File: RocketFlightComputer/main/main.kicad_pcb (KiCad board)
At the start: 4 copper layers, 53.7 x 53.7 mm, 148 parts, among them J1 BATT, Q2 SI2302, Q3 SI2302, Q4 SI2302, Y1 32.768kHz, Y2 24MHz, Y3 32.768kHz, Y4 32.768kHz

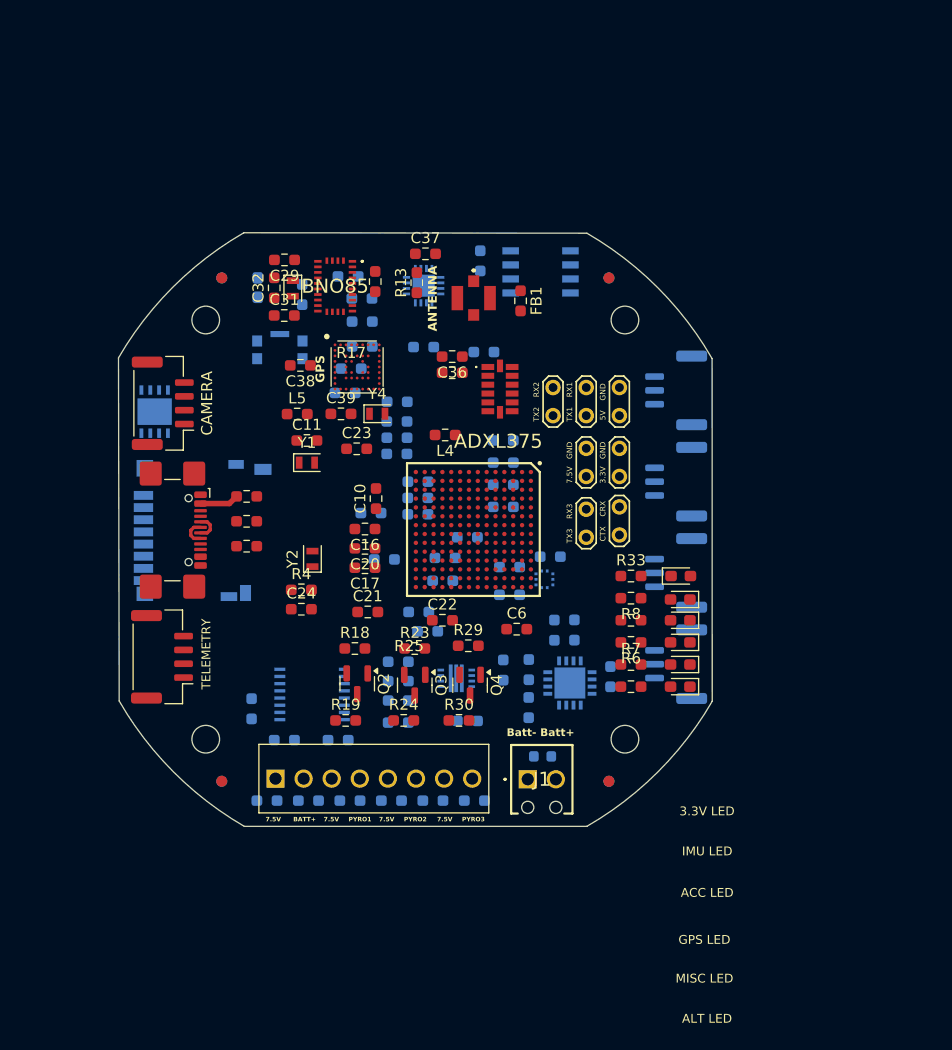
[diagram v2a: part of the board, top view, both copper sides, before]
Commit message: Preliminary layout done but need to rearrange sd card and such to have the best routing
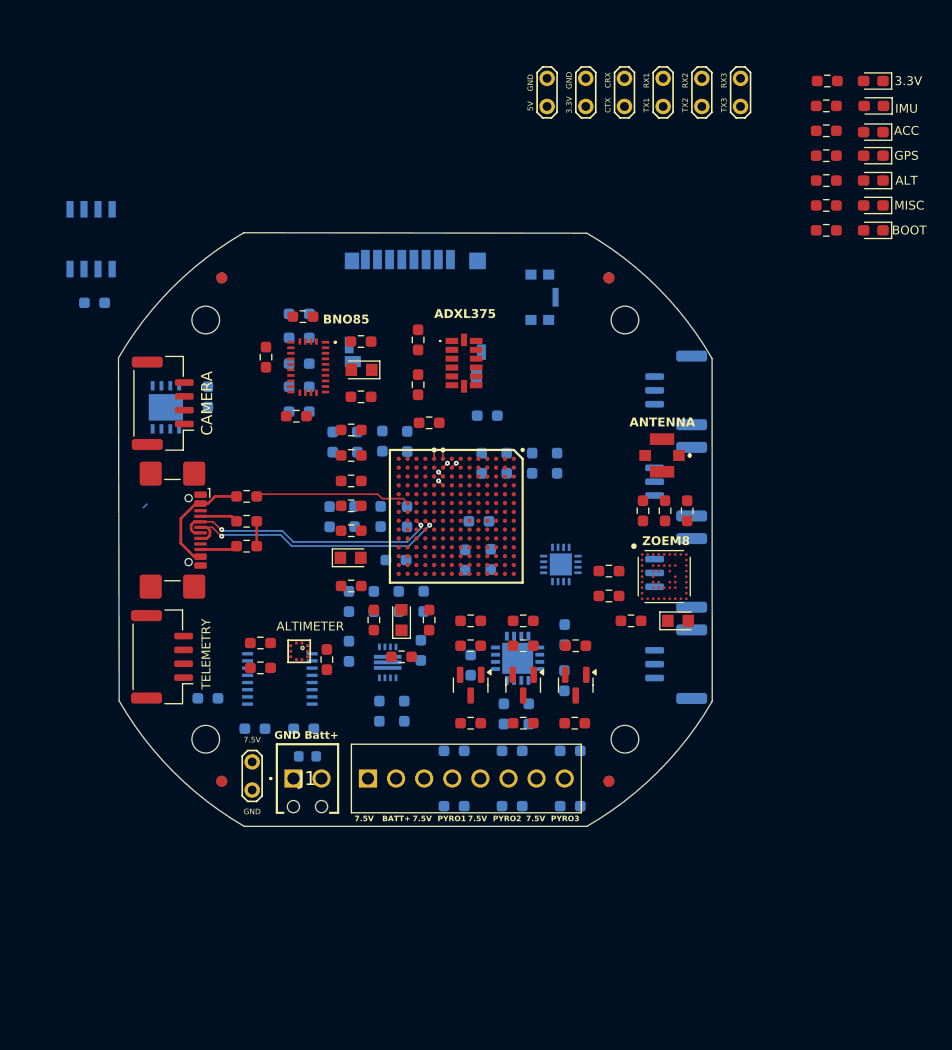
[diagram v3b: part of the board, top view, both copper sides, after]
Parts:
- BMP390, C33, C34, D1, R11, R2, R35: moved to F.Cu
- U-BLOX_ZOE_M8Q-0-10: value GPS -> ZOEM8
- Y1, Y2, Y3, Y4: footprint Crystal:Crystal_SMD_2012-2Pin_2.0x1.2mm -> footprint:830050789
- moved D1 58.7 mm to (151.3, 18.0), turned to 180 degrees
- moved R2 51.2 mm to (147.1, 18.0), turned to 0 degrees
- moved R5 46.9 mm to (147.0, 29.2)
- moved D4 46.9 mm to (151.3, 29.2)
- moved R33 46.0 mm to (147.0, 20.2)
- moved D8 45.9 mm to (151.3, 20.2), turned to 180 degrees
- moved R8 45.8 mm to (147.0, 22.5)
- moved D2 45.7 mm to (151.3, 22.6)
- moved R3 45.6 mm to (147.0, 24.7)
- moved D3 45.5 mm to (151.3, 24.7)
- moved R6 45.3 mm to (147.0, 27.0)
- moved D5 45.2 mm to (151.3, 27.0)
- moved R7 43.0 mm to (147.0, 31.5)
- moved D6 43.0 mm to (151.3, 31.5)
- moved TP6 41.4 mm to (139.3, 20.3)
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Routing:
- net /D+: track 2.44 -> 25.2 mm, vias 0 -> 2
- net /D-: track 2.44 -> 24.4 mm, vias 0 -> 2
- net Net-(MIMXRT1062DVL6B1-USB_OTG1_VBUS): track 0.00 -> 14.1 mm
- net Net-(L1-Pad1): track 3.52 -> 10.4 mm
- net Net-(USB_C_Receptacle_USB2.0_14P1-CC1): track 0.00 -> 3.44 mm
- net Net-(USB_C_Receptacle_USB2.0_14P1-CC2): track 0.00 -> 3.38 mm
- net GNDREF: track 0.00 -> 2.25 mm
- net /SD_B0_05: track 0.00 -> 1.00 mm, vias 0 -> 1
- net /SD_B0_03: track 0.00 -> 0.80 mm, vias 0 -> 1
- net /SD_B0_02: track 0.00 -> 0.80 mm, vias 0 -> 1
- net /SD_B0_04: track 0.00 -> 0.57 mm, vias 0 -> 1
- net /SD_B0_01: track 0.00 -> 0.57 mm, vias 0 -> 1
- net /SD_B0_00: track 0.00 -> 0.57 mm, vias 0 -> 1
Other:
- board text added: "3.3V"
- board text added: "ACC"
- board text added: "ALT"
- board text added: "BOOT"
- board text added: "GND"
- board text added: "GND Batt+"
- board text added: "GPS"
- board text added: "IMU"
- board text added: "MISC"
- board text removed: "3.3V LED"
- board text removed: "7.5V GND"
- board text removed: "ACC LED"
- board text removed: "ALT LED"
- board text removed: "Batt- Batt+"
- board text removed: "GPS LED"
- board text removed: "IMU LED"
- board text removed: "LED"
- board text removed: "MISC LED"

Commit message: Routing pcb
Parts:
- BMP390, C33, C34, R11: moved to B.Cu
- moved D8 75.9 mm to (97.3, 73.5)
- moved D2 72.7 mm to (97.3, 71.2), turned to 0 degrees
- moved R33 70.0 mm to (101.6, 73.5), turned to 180 degrees
- moved D3 69.8 mm to (97.3, 69.0), turned to 0 degrees
- moved D5 67.0 mm to (97.3, 66.7), turned to 0 degrees
- moved R8 66.7 mm to (101.6, 71.2), turned to 0 degrees
- moved R3 63.4 mm to (101.6, 69.0), turned to 0 degrees
- moved R6 60.4 mm to (101.6, 66.7), turned to 0 degrees
- moved C4 47.3 mm to (126.1, 51.8)
- moved 878-APS6404L-3SQR-SN1 46.9 mm to (125.1, 46.8)
- moved KMR241GLFS1 45.8 mm to (86.9, 68.0)
- moved D1 34.9 mm to (127.4, 43.4), turned to 0 degrees
- moved R2 34.9 mm to (123.2, 43.4)
- moved TP7 34.4 mm to (98.6, 36.8)
- moved TP3 31.1 mm to (95.4, 36.8)
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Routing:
- net /SD_B0_00: track 0.57 -> 21.4 mm
- net /SD_B0_01: track 0.57 -> 21.2 mm
- net /SD_B0_03: track 0.80 -> 20.6 mm
- net /SD_B0_02: track 0.80 -> 20.5 mm
- net /SD_B0_04: track 0.57 -> 19.2 mm
- net /SD_B0_05: track 1.00 -> 19.3 mm
- net GNDREF: track 2.25 -> 15.7 mm, vias 0 -> 2
- net Net-(MIMXRT1062DVL6B1-RTC_XTALI): track 0.00 -> 7.85 mm
- net Net-(U-BLOX_ZOE_M8Q-0-10-V_CORE): track 0.00 -> 6.49 mm
- net Net-(C10-Pad2): track 0.00 -> 6.23 mm
- net +3.3V: track 0.00 -> 6.13 mm, vias 0 -> 2
- net Net-(D3-A): track 0.00 -> 2.53 mm
- net /3.3v_led: track 0.00 -> 2.51 mm
- net Net-(D2-A): track 0.00 -> 2.47 mm
- net Net-(D5-A): track 0.00 -> 2.46 mm
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
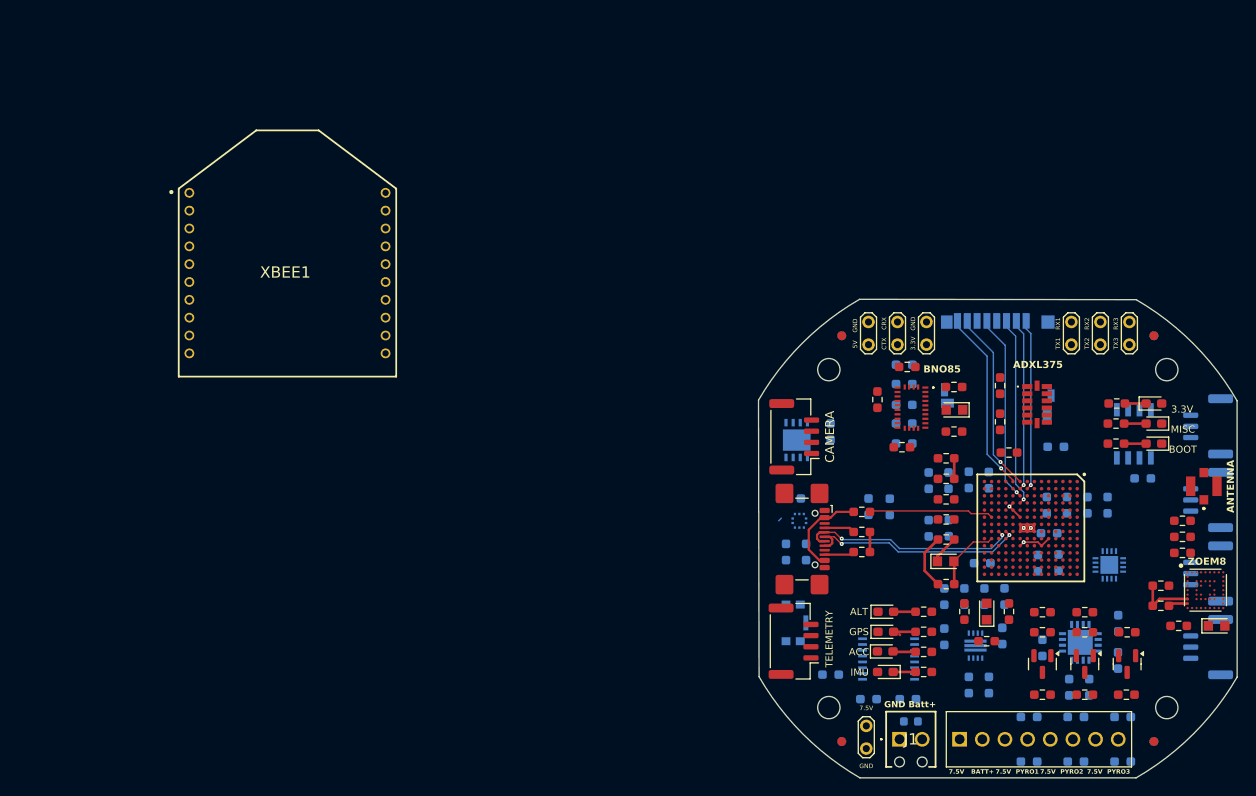
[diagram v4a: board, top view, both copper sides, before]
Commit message: Addition of teensy example and milestone on routing completed, missing a few components to connect
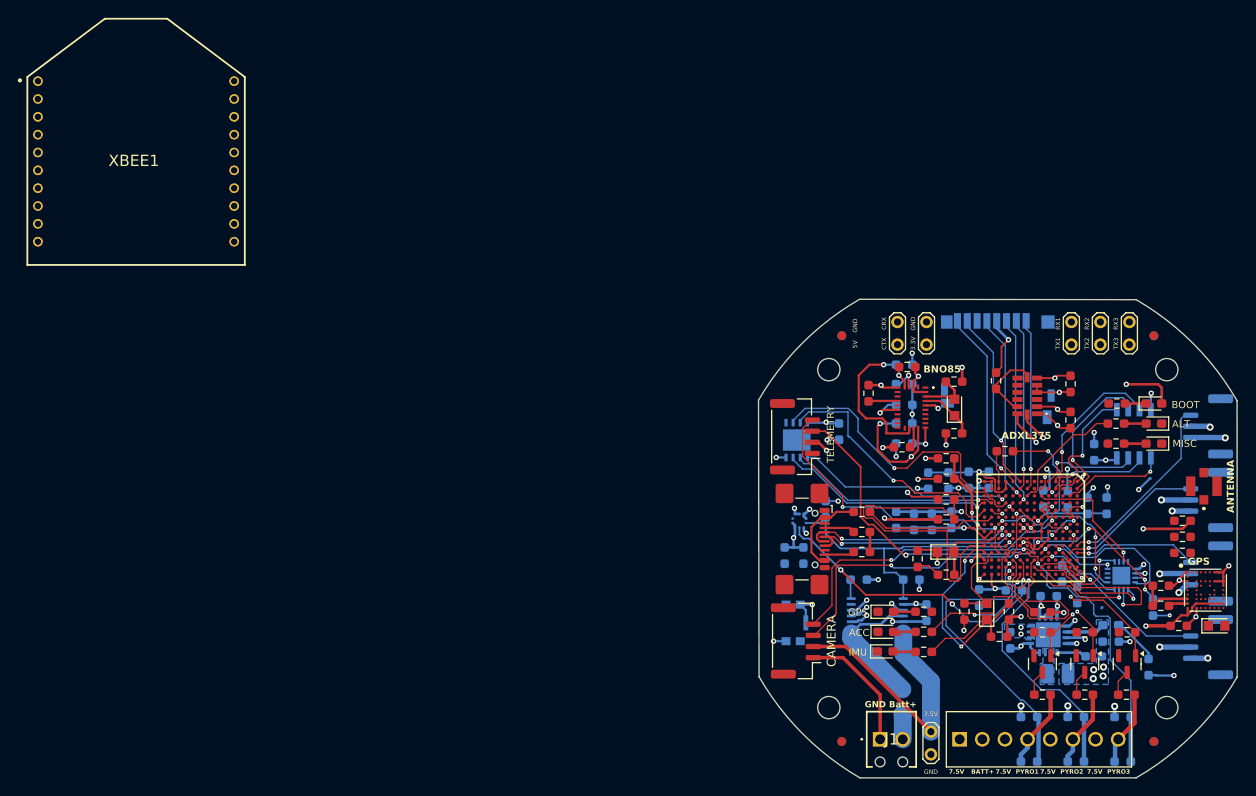
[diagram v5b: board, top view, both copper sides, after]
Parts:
- removed C41: 10uF, Resistor_SMD:R_0603_1608Metric_Pad0.98x0.95mm_HandSolder
- removed C42, C43: 22uF, Resistor_SMD:R_0603_1608Metric_Pad0.98x0.95mm_HandSolder
- removed C44: 3.3nF, Resistor_SMD:R_0603_1608Metric_Pad0.98x0.95mm_HandSolder
- removed L6: 1.5uH, Resistor_SMD:R_0603_1608Metric_Pad0.98x0.95mm_HandSolder
- removed R22: 470k, Resistor_SMD:R_0603_1608Metric_Pad0.98x0.95mm_HandSolder
- removed R25: 510k, Resistor_SMD:R_0603_1608Metric_Pad0.98x0.95mm_HandSolder
- removed R26: 82k, Resistor_SMD:R_0603_1608Metric_Pad0.98x0.95mm_HandSolder
- removed TP3: TestPoint_2Pole, TestPoint:TestPoint_2Pads_Pitch2.54mm_Drill0.8mm
- removed TPS621361RGXT1: 5Vreg, footprint:TPS621361RGXT
- C6, D8, R33: moved to B.Cu
- F2: value 5A -> 6A; footprint Fuse:Fuse_0603_1608Metric -> Fuse:Fuse_1206_3216Metric
- L2: footprint Resistor_SMD:R_0603_1608Metric_Pad0.98x0.95mm_HandSolder -> Inductor_SMD:L_1008_2520Metric_Pad1.43x2.20mm_HandSolder
- R14: moved to F.Cu
- R19, R24, R30: value 4 -> 7
- U-BLOX_ZOE_M8Q-0-10: value ZOEM8 -> GPS
- Y1, Y3: footprint footprint:830050789 -> Crystal:Crystal_SMD_2012-2Pin_2.0x1.2mm_HandSoldering
- moved D8 25.8 mm to (122.5, 68.2)
- moved R33 25.2 mm to (126.8, 72.9), turned to 90 degrees
- moved S4B-PH-K-S_LF__SN_1 22.9 mm to (87.1, 47.1)
- moved S4B-PH-K-S_LF__SN_2 22.9 mm to (87.2, 70.0)
- moved XBEE1 21.1 mm to (13.3, 0.25)
- moved R9 19.8 mm to (127.3, 66.3), turned to 90 degrees
- moved R166 14.5 mm to (94.3, 63.1), turned to 180 degrees
- moved R177 14.2 mm to (100.2, 63.1)
- moved C40 12.8 mm to (101.9, 66.8), turned to -90 degrees
- moved C6 12.0 mm to (107.8, 65.2), turned to -90 degrees
- moved R14 9.98 mm to (109.7, 40.8), turned to -90 degrees
- moved C35 8.97 mm to (118.0, 41.2), turned to -90 degrees
- moved C36 8.79 mm to (118.0, 45.2), turned to 90 degrees
- moved C3 8.38 mm to (115.6, 65.0), turned to 0 degrees
- moved R34 7.51 mm to (111.7, 64.3)
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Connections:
- C11 pad 1: GNDREF -> Net-(C10-Pad2)
- C11 pad 2: Net-(C10-Pad2) -> GNDREF
- C22 pad 1: Net-(MIMXRT1062DVL6B1-VDD_SNVS_CAP) -> GNDREF
- C22 pad 2: GNDREF -> Net-(MIMXRT1062DVL6B1-VDD_SNVS_CAP)
- C40 pad 1: +5V -> +3.3V
- INA260 pad 10: +5V -> +3.3V
- INA260 pad 7: /CURRENT VOLTAGE SENSOR/ALERT -> unconnected-(INA260-ALERT-Pad7)
- L4 pad 1: /M1M2 -> Net-(MIMXRT1062DVL6B1-DCDC_LP_1)
- L4 pad 2: Net-(MIMXRT1062DVL6B1-DCDC_LP_1) -> /M1M2
- MIMXRT1062DVL6B1 pad A10: unconnected-(MIMXRT1062DVL6B1-GPIO_B0_11-PadA10) -> /Servo4_PWM
- MIMXRT1062DVL6B1 pad A11: /Servo4_PWM -> /Servo2_PWM
- MIMXRT1062DVL6B1 pad C11: unconnected-(MIMXRT1062DVL6B1-GPIO_B1_02-PadC11) -> /Servo1_PWM
- MIMXRT1062DVL6B1 pad D9: /Servo2_PWM -> unconnected-(MIMXRT1062DVL6B1-GPIO_B0_10-PadD9)
- MIMXRT1062DVL6B1 pad E7: unconnected-(MIMXRT1062DVL6B1-GPIO_B0_01-PadE7) -> /PyroCH3_4
- MIMXRT1062DVL6B1 pad E8: unconnected-(MIMXRT1062DVL6B1-GPIO_B0_02-PadE8) -> /PyroCH2_3
- MIMXRT1062DVL6B1 pad G5: /PyroCH2_3 -> unconnected-(MIMXRT1062DVL6B1-GPIO_EMC_05-PadG5)
- MIMXRT1062DVL6B1 pad H3: /Servo1_PWM -> Net-(MIMXRT1062DVL6B1-GPIO_EMC_08)
- MIMXRT1062DVL6B1 pad H4: Net-(MIMXRT1062DVL6B1-GPIO_EMC_07) -> unconnected-(MIMXRT1062DVL6B1-GPIO_EMC_07-PadH4)
- MIMXRT1062DVL6B1 pad H5: /PyroCH3_4 -> unconnected-(MIMXRT1062DVL6B1-GPIO_EMC_06-PadH5)
- R10 pad 1: Net-(BNO85-BOOTN) -> +3.3V
- R10 pad 2: +3.3V -> Net-(BNO85-BOOTN)
- R12 pad 1: +3.3V -> Net-(BNO85-NRST)
- R12 pad 2: Net-(BNO85-NRST) -> +3.3V
- R3 pad 2: Net-(MIMXRT1062DVL6B1-GPIO_EMC_07) -> Net-(MIMXRT1062DVL6B1-GPIO_AD_B1_15)
- R5 pad 2: Net-(MIMXRT1062DVL6B1-GPIO_AD_B1_15) -> Net-(MIMXRT1062DVL6B1-GPIO_EMC_08)
- R8 pad 1: Net-(D2-A) -> Net-(MIMXRT1062DVL6B1-GPIO_AD_B1_14)
- R8 pad 2: Net-(MIMXRT1062DVL6B1-GPIO_AD_B1_14) -> Net-(D2-A)
- ScrewTerminal1 pad 1: /HighCurrentComponents/7.5V_AftSwitch -> +7.5V
- ScrewTerminal1 pad 2: +7.5V -> /HighCurrentComponents/7.5V_AftSwitch
- TPS62111RSAR1 pad 17: unconnected-(TPS62111RSAR1-EP-Pad17) -> GNDREF
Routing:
- net GNDREF: track 15.7 -> 175.0 mm, vias 2 -> 65
- net +7.5V: track 0.00 -> 134.6 mm, vias 0 -> 7
- net +3.3V: track 6.13 -> 101.2 mm, vias 2 -> 33
- net /Cam_TX: track 0.00 -> 40.8 mm, vias 0 -> 2
- net /BMP390_SDA1: track 0.00 -> 38.7 mm, vias 0 -> 3
- net Net-(MIMXRT1062DVL6B1-NVCC_PLL): track 0.00 -> 36.9 mm
- net /Cam_RX: track 0.00 -> 35.5 mm, vias 0 -> 2
- net /Pyro1_Test_40: track 0.00 -> 34.9 mm, vias 0 -> 1
- net /Xbee_RX: track 0.00 -> 34.4 mm, vias 0 -> 2
- net /BMO085_SCL: track 0.00 -> 33.8 mm, vias 0 -> 3
- net /BMP390_SCL1: track 0.00 -> 33.8 mm, vias 0 -> 1
- net /CLK: track 0.00 -> 33.6 mm, vias 0 -> 1
- net /Xbee_TX: track 0.00 -> 33.3 mm, vias 0 -> 2
- net Net-(MIMXRT1062DVL6B1-GPIO_AD_B1_14): track 0.00 -> 32.0 mm
- net /Pyro2_Test_41: track 0.00 -> 31.9 mm, vias 0 -> 1
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- added copper zone on B.Cu, net +3.3V
- added copper zone on In2.Cu, net +3.3V
- added copper zone on B.Cu, net +7.5V
- added copper zone on B.Cu, net Net-(TPS62111RSAR1-SW_1)

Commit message: First iteration of layout finished, we could call this v0, congratulations! Need an expert to state if layer 4 and layer 3 interations are ok (pwm/ psram/i2c/uart vs power plane 7.5v and 3.3v )
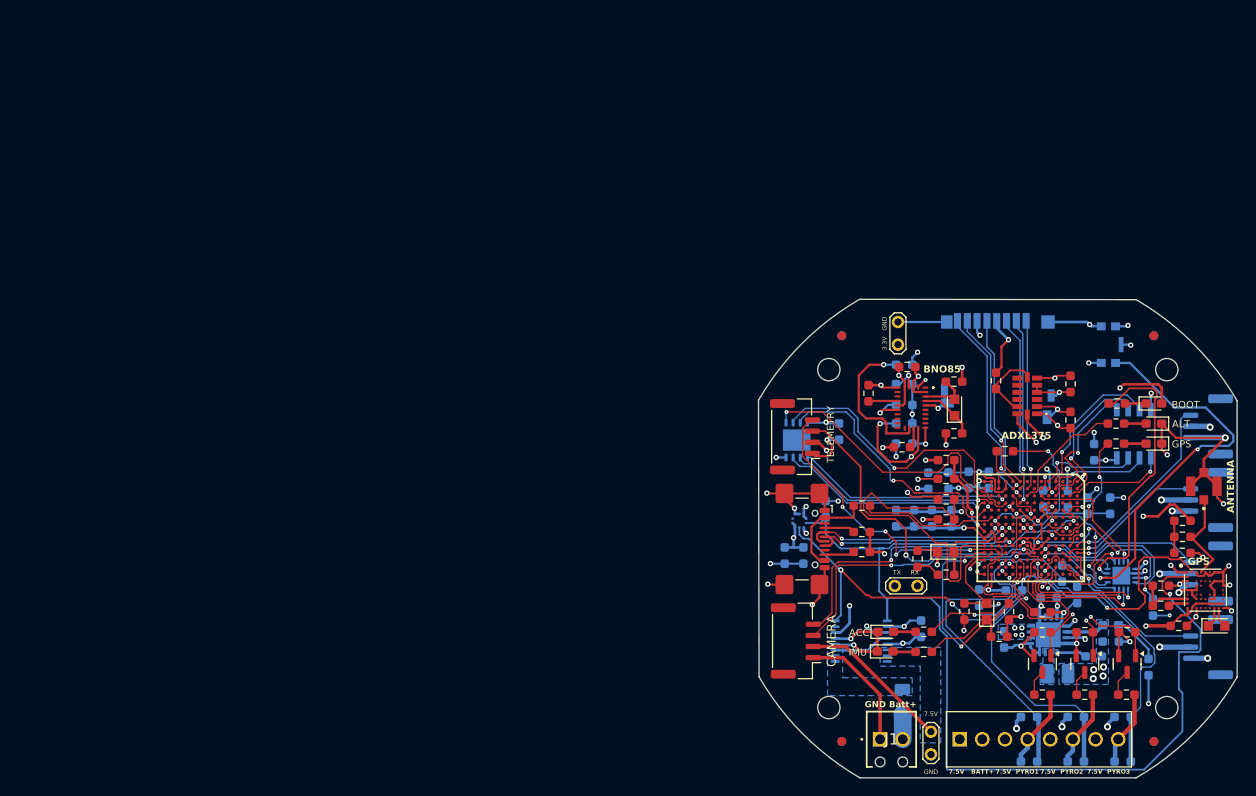
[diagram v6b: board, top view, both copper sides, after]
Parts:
- removed D5: GPS LED, LED_SMD:LED_0603_1608Metric_Pad1.05x0.95mm_HandSolder
- removed R166, R177: 10K, Resistor_SMD:R_0603_1608Metric_Pad0.98x0.95mm_HandSolder
- removed R6: 470, Resistor_SMD:R_0603_1608Metric_Pad0.98x0.95mm_HandSolder
- removed TP4, TP6, TP7: TestPoint_2Pole, TestPoint:TestPoint_2Pads_Pitch2.54mm_Drill0.8mm
- removed XBEE1: XB24CAPIT-001, footprint:XB24CAPIT-001
- D3: value 200G ACC LED -> GPS
- D6: value Misc LED -> 200G ACC LED
- moved KMR241GLFS1 47.2 mm to (122.3, 36.8)
- moved TP5 35.5 mm to (98.3, 63.8), turned to 0 degrees
- moved TP1 3.20 mm to (98.7, 36.8)
- moved INA260 3.08 mm to (94.6, 70.0)
- moved C40 1.90 mm to (101.3, 68.6)
- moved C1 0.71 mm to (110.6, 69.8)
- moved L1 0.70 mm to (94.6, 54.8)
- moved C14 0.40 mm to (102.5, 56.3)
- moved C28 0.40 mm to (122.5, 54.9)
- moved C9 0.40 mm to (100.5, 56.3)
- moved C16 0.21 mm to (104.1, 49.7)
- moved C7 0.18 mm to (98.5, 56.3)
- moved C18 0.17 mm to (104.7, 56.3)
- moved C3 0.15 mm to (115.6, 65.1)
- turned C13 to -90 degrees
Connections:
- net /Reserve_RX2 renamed /Reserve_RX
- net /Reserve_TX2 renamed /Reserve_TX
- MIMXRT1062DVL6B1 pad C10: Net-(MIMXRT1062DVL6B1-GPIO_B0_12) -> unconnected-(MIMXRT1062DVL6B1-GPIO_B0_12-PadC10)
- MIMXRT1062DVL6B1 pad H13: /Reserve_CTX -> unconnected-(MIMXRT1062DVL6B1-GPIO_AD_B1_08-PadH13)
- MIMXRT1062DVL6B1 pad J13: /Reserve_RX1 -> unconnected-(MIMXRT1062DVL6B1-GPIO_AD_B1_11-PadJ13)
- MIMXRT1062DVL6B1 pad L11: /Reserve_TX3 -> unconnected-(MIMXRT1062DVL6B1-GPIO_AD_B1_02-PadL11)
- MIMXRT1062DVL6B1 pad L13: /Reserve_TX1 -> unconnected-(MIMXRT1062DVL6B1-GPIO_AD_B1_10-PadL13)
- MIMXRT1062DVL6B1 pad M12: /Reserve_RX3 -> unconnected-(MIMXRT1062DVL6B1-GPIO_AD_B1_03-PadM12)
- MIMXRT1062DVL6B1 pad M13: /Reserve_CRX -> unconnected-(MIMXRT1062DVL6B1-GPIO_AD_B1_09-PadM13)
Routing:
- net GNDREF: track 175.0 -> 297.4 mm, vias 65 -> 83
- net /BMP390_SCL1: track 33.8 -> 113.1 mm, vias 1 -> 2
- net Net-(KMR241GLFS1-COM_1): track 0.00 -> 42.5 mm, vias 0 -> 2
- net Net-(MKL02Z32VFG4-PTB3/IRQ_10): track 0.00 -> 31.2 mm, vias 0 -> 1
- net /D0: track 0.00 -> 30.9 mm, vias 0 -> 1
- net /BMP390_SDA1: track 38.7 -> 68.3 mm, vias 3 -> 4
- net /Reserve_TX: track 0.00 -> 20.4 mm, vias 0 -> 1
- net Net-(MIMXRT1062DVL6B1-VDD_USB_CAP): track 0.00 -> 19.3 mm, vias 0 -> 2
- net /Reserve_RX: track 0.00 -> 17.3 mm, vias 0 -> 1
- net Net-(MIMXRT1062DVL6B1-GPIO_B0_03): track 0.00 -> 14.3 mm, vias 0 -> 2
- net +7.5V: track 134.6 -> 122.1 mm, vias 7 -> 9
- net /PTA3: track 19.3 -> 30.2 mm, vias 4 -> 6
- net /GPS ZOEM8/ANT: track 0.00 -> 10.7 mm
- net +BATT: track 15.3 -> 6.42 mm
- net Net-(C37-Pad1): track 0.00 -> 3.60 mm
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- added copper zone on B.Cu, net +BATT
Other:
- board text added: "TX RX"
- board text removed: "5V GND"
- board text removed: "CTX CRX"
- board text removed: "MISC"
- board text removed: "TX1 RX1"
- board text removed: "TX2 RX2"
- board text removed: "TX3 RX3"
